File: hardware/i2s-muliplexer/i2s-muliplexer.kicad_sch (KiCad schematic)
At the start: 31 parts, among them J1 Conn_01x05, J2 Conn_01x05, J3 Conn_01x05, J4 Conn_01x05, J5 Conn_01x05, J6 Conn_01x05, J7 Conn_01x07, J8 Conn_01x05, U1 74HC244, U2 74HC244, U3 74HC244, U4 74HC126, U5 74LS138

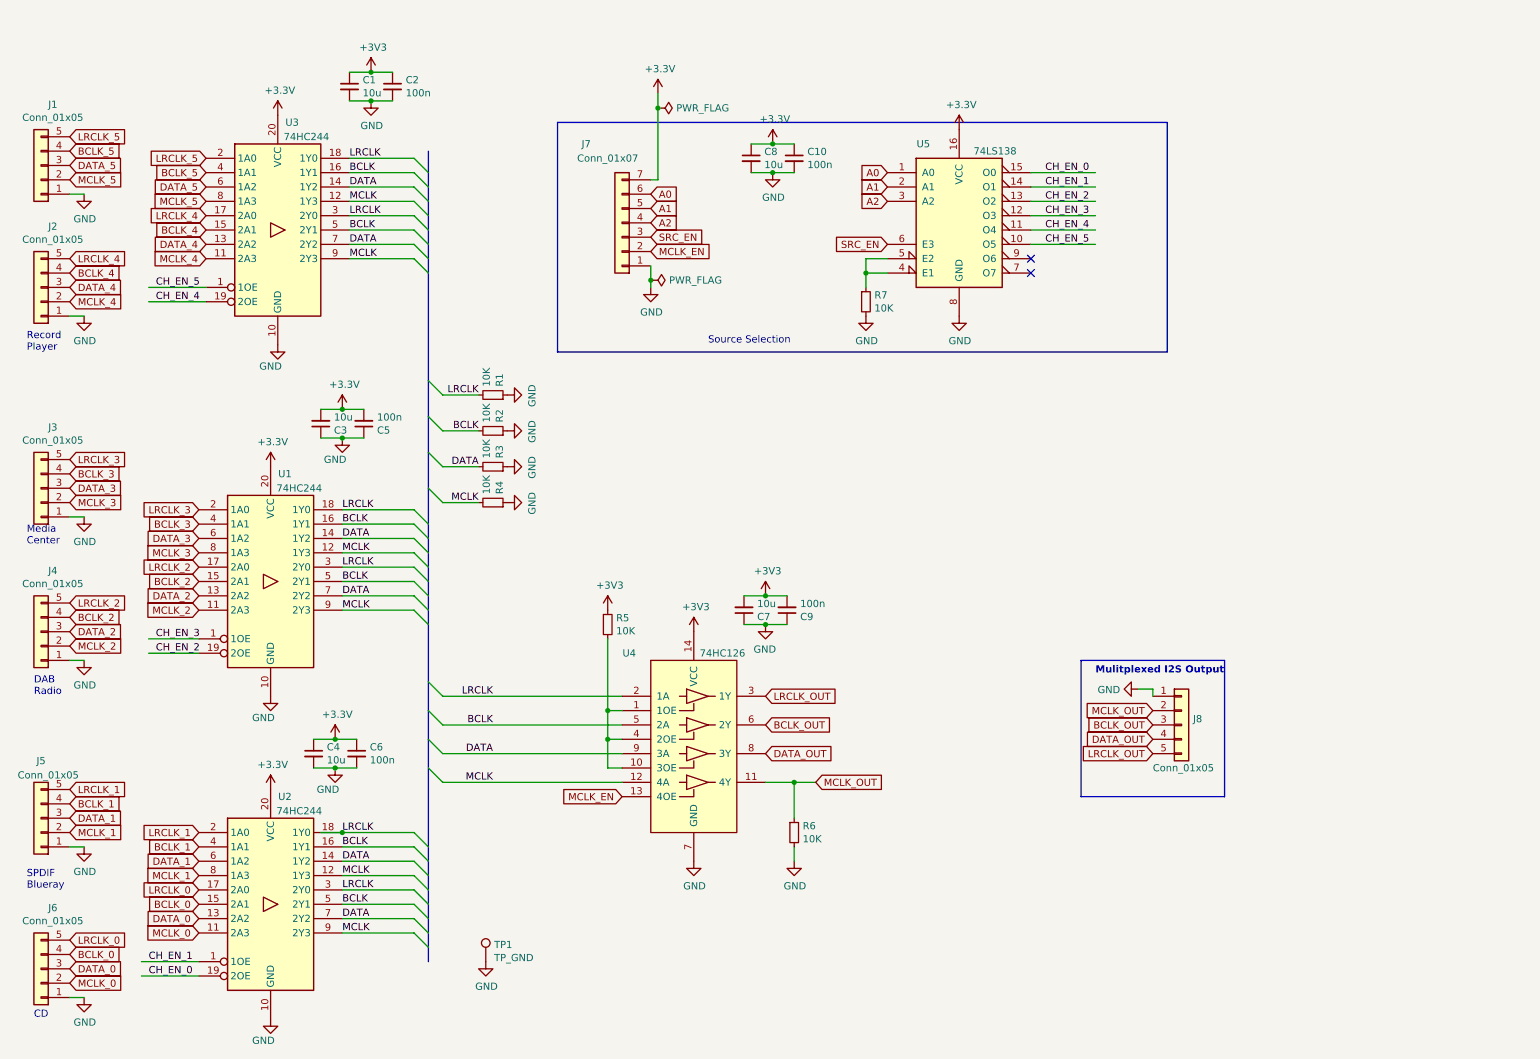
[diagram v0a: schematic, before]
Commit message: Layout with double row connectors
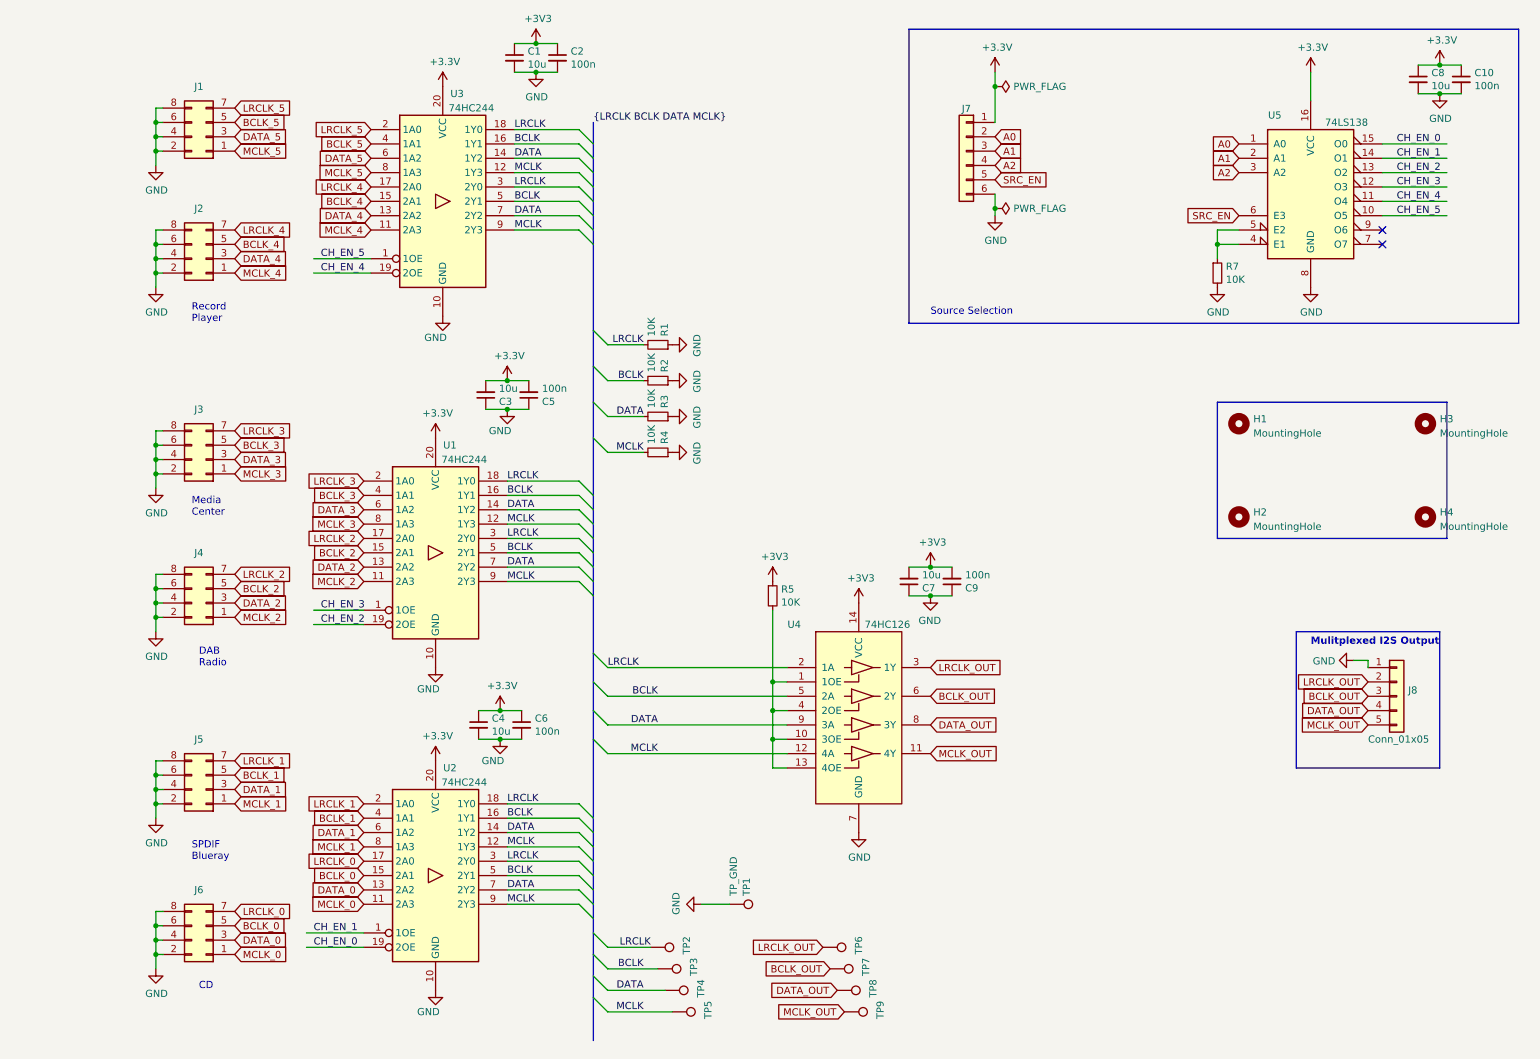
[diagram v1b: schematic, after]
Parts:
- removed J1, J2, J3, J4, J5, J6: Conn_01x05, Connector_PinHeader_2.54mm:PinHeader_1x05_P2.54mm_Vertical, symbol Connector_Generic:Conn_01x05
- removed J7: Conn_01x07, Connector_PinHeader_2.54mm:PinHeader_1x07_P2.54mm_Vertical, symbol Connector_Generic:Conn_01x07
- removed R6: 10K, Resistor_SMD:R_0805_2012Metric_Pad1.15x1.40mm_HandSolder, symbol Device:R_Small
- added H1, H2, H3, H4: MountingHole, MountingHole:MountingHole_3.2mm_M3_DIN965, symbol Mechanical:MountingHole
- added J1, J2, J3, J4, J5, J6: Conn_02x04_Odd_Even, Connector_PinHeader_2.54mm:PinHeader_2x04_P2.54mm_Vertical, symbol Connector_Generic:Conn_02x04_Odd_Even
- added J7: Conn_01x06, Connector_PinHeader_2.54mm:PinHeader_1x06_P2.54mm_Vertical, symbol Connector_Generic:Conn_01x06
- added TP2, TP3, TP4, TP5, TP6, TP7, TP8, TP9: TestPoint, TestPoint:TestPoint_Pad_2.0x2.0mm, symbol Connector:TestPoint
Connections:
- net MCLK_EN is gone; now on an unnamed net: U4.13 (4OE)
- net +3V3: now also J7.1 (Pin_1)
- net A0: now also J7.2 (Pin_2)
- net A1: now also J7.3 (Pin_3)
- net A2: now also J7.4 (Pin_4)
- net BCLK: now also TP3.1
- net BCLK_0: now also J6.5 (Pin_5)
- net BCLK_1: now also J5.5 (Pin_5)
- net BCLK_2: now also J4.5 (Pin_5)
- net BCLK_3: now also J3.5 (Pin_5)
- net BCLK_4: now also J2.5 (Pin_5)
- net BCLK_5: now also J1.5 (Pin_5)
- net BCLK_OUT: now also TP7.1
- net DATA: now also TP4.1
- net DATA_0: now also J6.3 (Pin_3)
- net DATA_1: now also J5.3 (Pin_3)
- net DATA_2: now also J4.3 (Pin_3)
- net DATA_3: now also J3.3 (Pin_3)
- net DATA_4: now also J2.3 (Pin_3)
- net DATA_5: now also J1.3 (Pin_3)
- net DATA_OUT: now also TP8.1
- net GND: now also J1.2 (Pin_2), J1.4 (Pin_4), J1.6 (Pin_6), J1.8 (Pin_8), J2.2 (Pin_2), J2.4 (Pin_4), J2.6 (Pin_6), J2.8 (Pin_8), J3.2 (Pin_2), J3.4 (Pin_4), J3.6 (Pin_6), J3.8 (Pin_8), J4.2 (Pin_2), J4.4 (Pin_4), J4.6 (Pin_6), J4.8 (Pin_8), J5.2 (Pin_2), J5.4 (Pin_4), J5.6 (Pin_6), J5.8 (Pin_8), J6.2 (Pin_2), J6.4 (Pin_4), J6.6 (Pin_6), J6.8 (Pin_8), J7.6 (Pin_6)
- net LRCLK: now also TP2.1
- net LRCLK_0: now also J6.7 (Pin_7)
- net LRCLK_1: now also J5.7 (Pin_7)
- net LRCLK_2: now also J4.7 (Pin_7)
- net LRCLK_3: now also J3.7 (Pin_7)
- net LRCLK_4: now also J2.7 (Pin_7)
- net LRCLK_5: now also J1.7 (Pin_7)
- net LRCLK_OUT: now also J8.2 (Pin_2), TP6.1; no longer J8.5 (Pin_5)
- net MCLK: now also TP5.1
- net MCLK_0: now also J6.1 (Pin_1)
- net MCLK_1: now also J5.1 (Pin_1)
- net MCLK_2: now also J4.1 (Pin_1)
- net MCLK_3: now also J3.1 (Pin_1)
- net MCLK_4: now also J2.1 (Pin_1)
- net MCLK_5: now also J1.1 (Pin_1)
- net MCLK_OUT: now also J8.5 (Pin_5), TP9.1; no longer J8.2 (Pin_2)
- net SRC_EN: now also J7.5 (Pin_5)
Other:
- moved on the sheet: C1, C10, C2, C3, C4, C5, C6, C7, C8, C9, J8, R1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
